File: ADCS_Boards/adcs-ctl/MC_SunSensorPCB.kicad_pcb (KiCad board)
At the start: 4 copper layers, 90.2 x 95.9 mm, 120 parts, among them J1 PC104_Connector, J2 PMOD, J3 Conn_01x03_Female, Q12 20V/0.2A/8MHz/1.2Ω/1Vth, Q14 20V/0.2A/8MHz/1.2Ω/1Vth, Q3 20V/0.2A/8MHz/1.2Ω/1Vth, Q4 20V/0.2A/8MHz/1.2Ω/1Vth, Q6 20V/0.2A/8MHz/1.2Ω/1Vth, Q9 20V/0.2A/8MHz/1.2Ω/1Vth, U1 9DoF IMU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

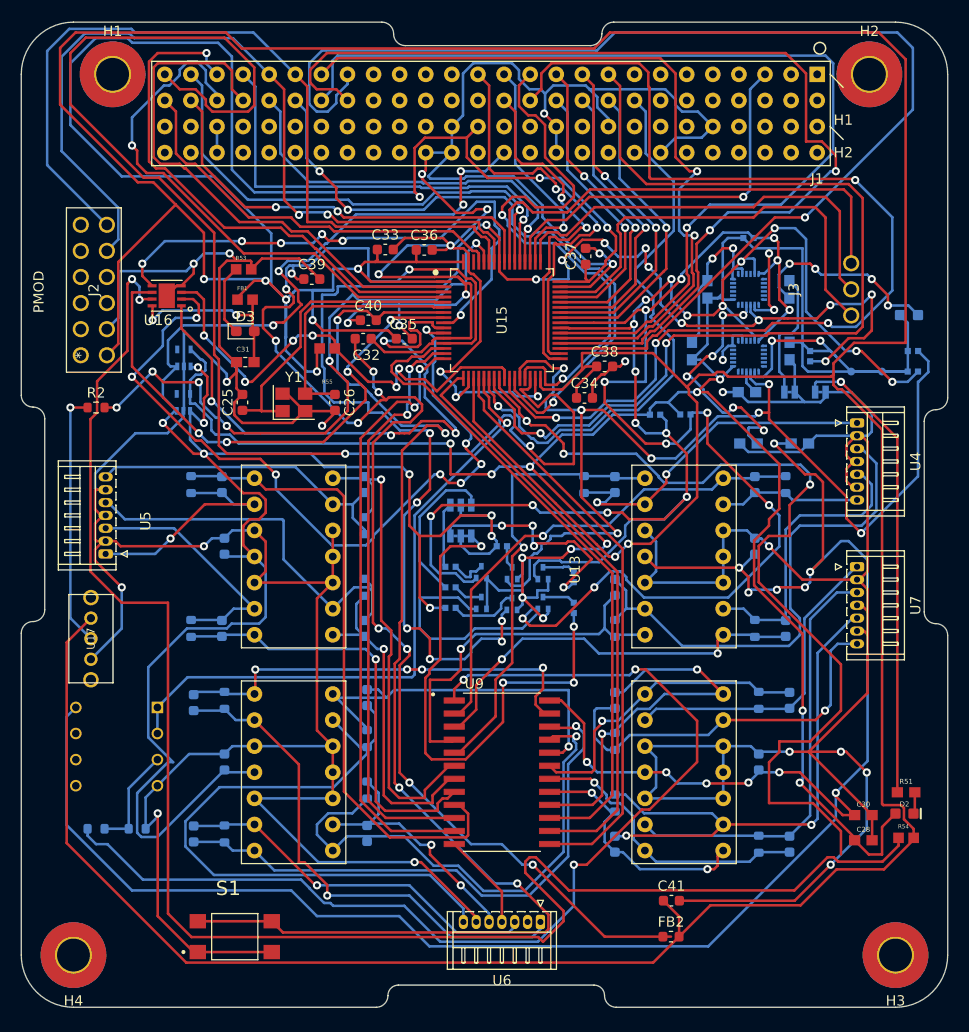
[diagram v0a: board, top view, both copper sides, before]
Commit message: adcs: udpated rwl-db and adcs-ctl on behalf of Yasin
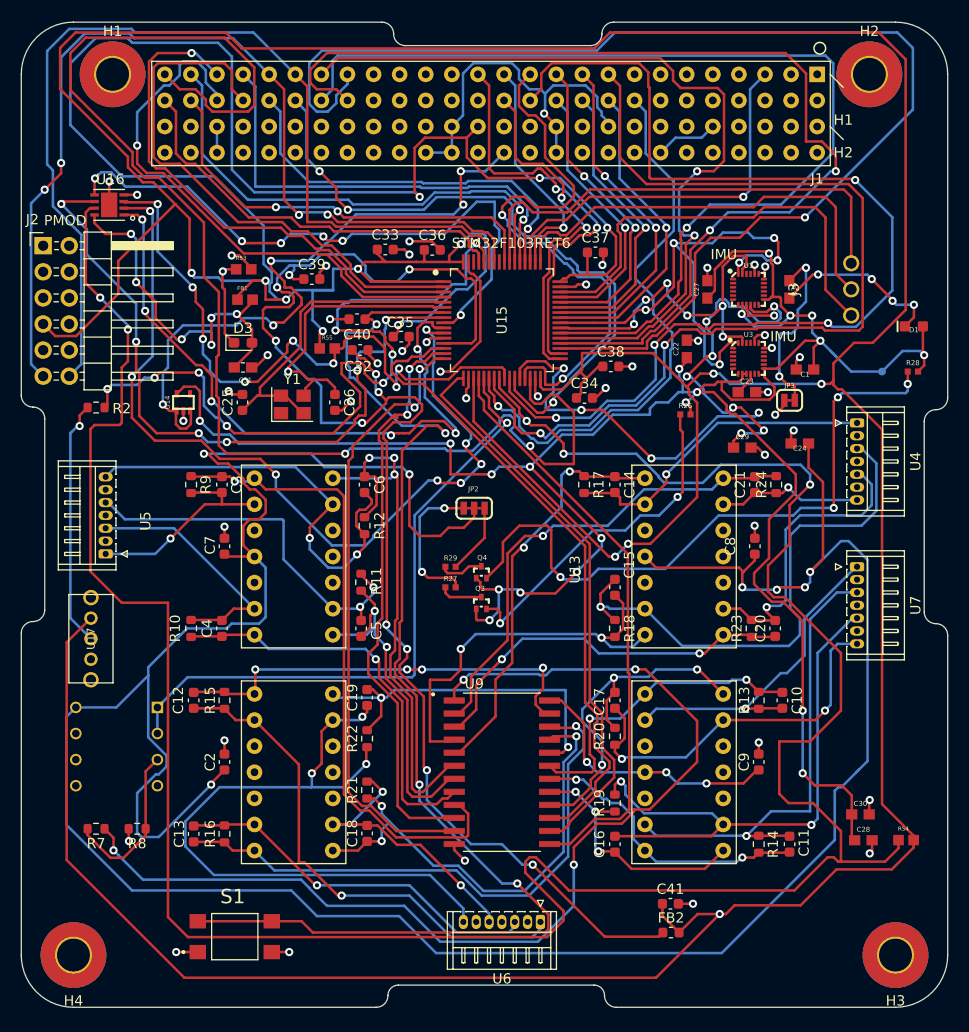
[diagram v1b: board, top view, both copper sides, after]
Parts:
- removed D2: RED, SparkFun_IMU_Breakout_ICM-20948:LED-0603
- removed JP5: I2C PU, SparkFun_IMU_Breakout_ICM-20948:SMT-JUMPER_3_2-NC_TRACE_SILK
- removed JP6: LED, SparkFun_IMU_Breakout_ICM-20948:SMT-JUMPER_2_NC_TRACE_SILK
- removed Q12, Q14, Q6, Q9: 20V/0.2A/8MHz/1.2Ω/1Vth, SparkFun_IMU_Breakout_ICM-20948:SOT-416FL
- removed R1, R3, R32, R33, R40, R43, R46, R47: 2.2k, SparkFun_IMU_Breakout_ICM-20948:0402-TIGHT
- removed R51: 220, SparkFun_IMU_Breakout_ICM-20948:0603
- removed TP2: 1.8V, SparkFun_IMU_Breakout_ICM-20948:PAD.03X.03
- removed U2: 1.8V/100mA, SparkFun_IMU_Breakout_ICM-20948:SC70
- C1, C22, C23, C24, C27, C29, D1, JP2, JP3, Q3, Q4, R26, R27, R28, R29, R36, R7, R8, U1, U14, U3: moved to F.Cu
- C10, C11, C12, C13, C14, C15, C16, C17, C18, C19, C20, C21, C3, C4, C5, C6: value C -> 180pF; moved to F.Cu
- C2, C7, C8, C9: value C -> 100nF; moved to F.Cu
- C25, C26: value 10p -> 10pF
- C31, C32, C34, C35, C36, C37, C38: value 100n -> 100nF
- C33: value 10u -> 10uF
- C39: value 10n -> 10nF
- C40, C41: value 1u -> 1uF
- J2: value PMOD -> PPTC062LJBN-RC; footprint Footprints_QSAT:PPTC062LJBN-RC -> Connector_PinHeader_2.54mm:PinHeader_2x06_P2.54mm_Horizontal
- R10, R11, R12, R13, R14, R15, R16, R17, R18, R19, R20, R21, R22, R23, R24, R9: value R -> 5.76k; moved to F.Cu
- moved J2 11.3 mm to (111.3, 68.8), turned to 0 degrees
- moved U16 10.5 mm to (117.8, 64.8)
- moved C1 2.34 mm to (185.5, 80.8), turned to 180 degrees
- moved JP2 1.33 mm to (153.3, 94.3), turned to 0 degrees
- moved D1 1.20 mm to (196.1, 76.6), turned to 180 degrees
- moved D3 1.14 mm to (130.8, 78.2)
- moved C40 1.14 mm to (142.2, 78.9)
- moved C32 1.10 mm to (141.9, 75.9)
- moved C37 1.02 mm to (165.1, 69.4), turned to 0 degrees
- moved C20 1.02 mm to (182.6, 106.0)
- moved R24 0.92 mm to (182.7, 92.0)
- moved JP3 0.80 mm to (184.0, 83.8), turned to 0 degrees
- moved C36 0.78 mm to (149.2, 69.2)
- moved C29 0.72 mm to (179.4, 88.4), turned to 0 degrees
- moved C10 0.70 mm to (183.3, 113.0)
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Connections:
- C30 pad 1: +5V -> 1.8V
- Q3 pad 2: IMU_SDA -> /SDA/SDI
- Q4 pad 2: IMU_SCL -> /SCL/SCLK
- R26 pad 1: IMU_SDA -> /SDA/SDI
- R28 pad 1: IMU_SCL -> /SCL/SCLK
- U1 pad 9: /AD0/SDO_2 -> GND
- U15 pad 28: /AD0/SDO -> PB2
- U15 pad 57: /AD0/SDO_2 -> PB5
- U3 pad 9: /AD0/SDO -> 1.8V
- Y1 pad 1: RCC_OSC_IN -> unconnected-(Y1-Pad1)
- Y1 pad 2: GND -> RCC_OSC_IN
- Y1 pad 4: GND -> RCC_OSC_IN
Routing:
- net GND: track 692.1 -> 133.5 mm, vias 31 -> 45
- net /AD0/SDO_2: track 144.6 -> 0.00 mm, vias 17 -> 0
- net IMU_SCL: track 142.4 -> 34.7 mm, vias 16 -> 6
- net /AD0/SDO: track 106.3 -> 0.00 mm, vias 7 -> 0
- net IMU_SDA: track 136.8 -> 52.4 mm, vias 11 -> 6
- net /SCL/SCLK: track 0.00 -> 64.1 mm, vias 0 -> 4
- net Net-(JP5-Pad1): track 52.4 -> 0.00 mm, vias 4 -> 0
- net +5V: track 414.7 -> 368.0 mm, vias 24 -> 15
- net Net-(JP6-Pad2): track 45.7 -> 0.00 mm, vias 1 -> 0
- net 1.8V: track 263.6 -> 228.1 mm, vias 16 -> 20
- net PB2: track 0.00 -> 35.1 mm, vias 0 -> 4
- net /SDA/SDI: track 0.00 -> 33.2 mm, vias 0 -> 2
- net Net-(JP5-Pad3): track 22.6 -> 0.00 mm, vias 4 -> 0
- net Net-(C31-Pad2): track 18.0 -> 35.9 mm, vias 2 -> 6
- net SPI1_SCK: track 52.2 -> 69.4 mm, vias 4 -> 6
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
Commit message: Update adcs-ctl for yasin
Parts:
- added C42: 10uF, SparkFun_IMU_Breakout_ICM-20948:0603, F.Cu at (178.6, 140.7)
- added C43: 10uF, SparkFun_IMU_Breakout_ICM-20948:0603, F.Cu at (174.8, 140.7)
- added TP2: 3V3, SparkFun_IMU_Breakout_ICM-20948:PAD.03X.03, F.Cu at (191.6, 134.1)
- added U2: BU33SA5WGWZ-E2, Footprints_QSAT:BU33SA5WGWZ-E2, F.Cu at (184.2, 137.7)
- J2: footprint Connector_PinHeader_2.54mm:PinHeader_2x06_P2.54mm_Horizontal -> Connector_PinSocket_2.54mm:PinSocket_2x06_P2.54mm_Horizontal
- moved J2 11.0 mm to (122.3, 68.5)
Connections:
- J1 pad 79: +3V3 -> unconnected-(J1-Pad79)
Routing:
- net Net-(J1-Pad43): track 92.9 -> 105.7 mm, vias 4 -> 5
- net +5V: track 368.0 -> 375.0 mm, vias 15 -> 16
- net Net-(C31-Pad2): track 35.9 -> 42.1 mm, vias 6 -> 4
- net Net-(J1-Pad41): track 95.5 -> 100.3 mm, vias 0 -> 1
- net GND: track 133.5 -> 137.4 mm, vias 45 -> 48
- net SPI1_MISO: track 84.9 -> 88.7 mm
- net /BOOT0: track 75.3 -> 71.5 mm
- net SPI1_SCK: track 69.4 -> 72.6 mm
- net +3V3: track 631.3 -> 633.6 mm
- net GPIO2: track 63.4 -> 64.5 mm
- net SPI1_NSS: track 64.2 -> 65.1 mm, vias 6 -> 5
- net GPIO1: track 256.6 -> 255.9 mm, vias 5 -> 3

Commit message: adcs: split adcs-ctl board power layer between 5v 3v3 and 1v8
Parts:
- removed JP2: I2C PU, SparkFun_IMU_Breakout_ICM-20948:SMT-JUMPER_3_2-NC_TRACE_SILK
- removed JP3: LED, SparkFun_IMU_Breakout_ICM-20948:SMT-JUMPER_2_NC_TRACE_SILK
- TP1: moved to F.Cu
- moved C43 80.9 mm to (194.7, 62.2)
- moved C41 72.1 mm to (194.8, 64.3)
- moved FB2 70.6 mm to (134.5, 76.1)
- moved U14 62.1 mm to (187.1, 86.5)
- moved C42 57.4 mm to (125.8, 118.2)
- moved C30 54.0 mm to (196.5, 70.4)
- moved C28 53.5 mm to (196.5, 73.4)
- moved Q4 49.5 mm to (197.4, 76.1)
- moved Q3 49.5 mm to (197.2, 79.0)
- moved R27 48.3 mm to (194.9, 81.9), turned to -90 degrees
- moved R29 46.6 mm to (193.9, 81.9), turned to -90 degrees
- moved R26 23.5 mm to (197.1, 81.9), turned to -90 degrees
- moved U2 20.6 mm to (191.4, 118.4)
- moved TP2 10.7 mm to (191.9, 123.3)
- moved D1 9.90 mm to (194.7, 66.8)
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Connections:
- Q3 pad 3: /SDA/SDI_VIN -> IMU_SDA
- Q4 pad 3: /SCL/SCLK_VIN -> IMU_SCL
- R27 pad 1: /SDA/SDI_VIN -> IMU_SDA
- R27 pad 2: Net-(JP2-Pad1) -> +3V3
- R29 pad 1: /SCL/SCLK_VIN -> IMU_SCL
- R29 pad 2: Net-(JP2-Pad3) -> +3V3
- R36 pad 1: Net-(JP3-Pad2) -> GND
- U1 pad 23: IMU_SCL -> /SCL/SCLK
- U1 pad 24: IMU_SDA -> /SDA/SDI
- U3 pad 23: IMU_SCL -> /SCL/SCLK
- U3 pad 24: IMU_SDA -> /SDA/SDI
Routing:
- net +3V3: track 633.6 -> 82.5 mm, vias 15 -> 22
- net +5V: track 375.0 -> 29.7 mm, vias 16 -> 15
- net 1.8V: track 228.1 -> 24.2 mm, vias 20 -> 14
- net +3.3VA: track 144.7 -> 64.5 mm, vias 11 -> 6
- net GND: track 137.4 -> 165.5 mm, vias 48 -> 93
- net GPIO1: track 255.9 -> 230.5 mm
- net PB0: track 104.5 -> 123.6 mm
- net Net-(JP3-Pad2): track 17.8 -> 0.00 mm, vias 2 -> 0
- net IMU_SCL: track 34.7 -> 51.1 mm, vias 6 -> 5
- net /SCL/SCLK: track 64.1 -> 47.9 mm
- net Net-(JP2-Pad1): track 14.3 -> 0.00 mm, vias 2 -> 0
- net Net-(JP2-Pad3): track 6.87 -> 0.00 mm
- net /SCL/SCLK_VIN: track 4.27 -> 0.00 mm
- net /SDA/SDI_VIN: track 4.22 -> 0.00 mm
- net /SDA/SDI: track 33.2 -> 36.7 mm, vias 2 -> 3
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- added copper zone on In2.Cu, net +3V3
- added copper zone on In2.Cu, net 1.8V

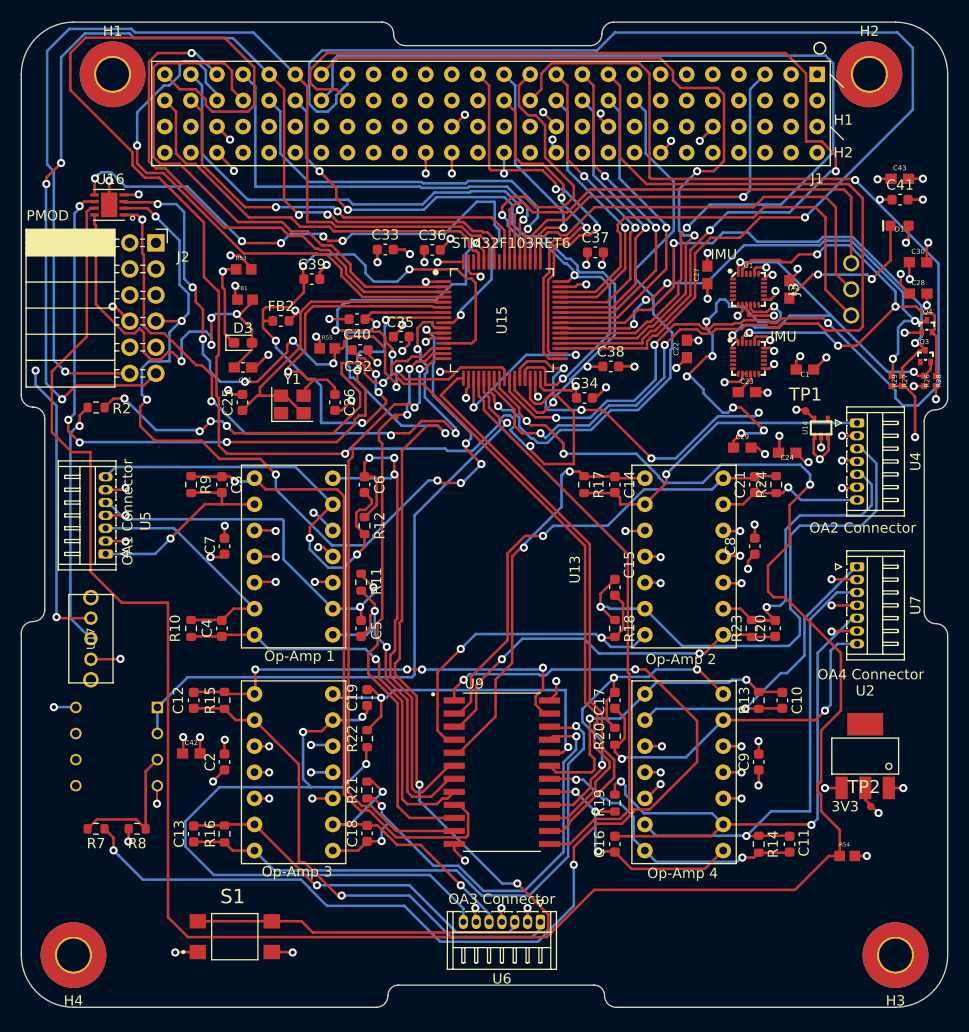
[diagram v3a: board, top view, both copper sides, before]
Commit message: adcs: adcs-ctl: continued silkscreen changes
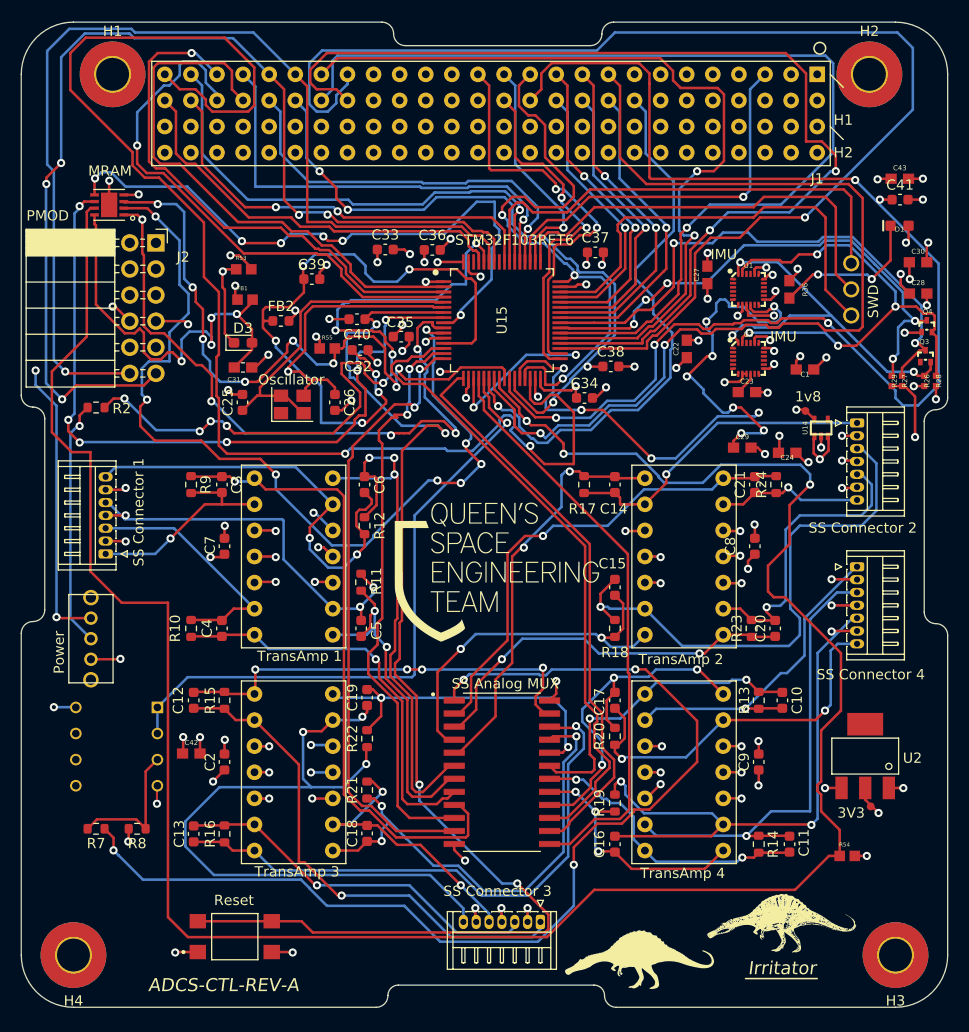
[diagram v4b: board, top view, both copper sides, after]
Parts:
- added G***: LOGO, LOGO, F.Cu at (183.3, 134.7)
- added G***: LOGO, LOGO, F.Cu at (155.6, 100.3)
- added G***: LOGO, LOGO, F.Cu at (169.4, 138.3)
- added G***: LOGO, LOGO, B.Cu at (175.3, 134.1)
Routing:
- net GND: track 165.5 -> 148.1 mm, vias 93 -> 83
- net +5V: track 29.7 -> 27.7 mm, vias 15 -> 14
- net Net-(C19-Pad2): track 36.2 -> 34.4 mm
- net +3V3: track 82.5 -> 83.3 mm
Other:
- board text added: "1v8"
- board text added: "ADCS-CTL-REV-A"
- board text added: "Alex MacQuarrie"
- board text added: "Ankylosaurus"
- board text added: "Irritator"
- board text added: "MRAM"
- board text added: "Oscillator"
- board text added: "Power"
- board text added: "Reset"
- board text added: "SS 3v3 Limiter"
- board text added: "SS Analog MUX"
- board text added: "SWD"
- board text added: "Yasin Shahrami Tony Jajcanin Aidan Darling Hatim Belhadjhamida Luke Parna-Gile Alex MacQuarrie Dylan Burke Sid Arya Aidan Sheedy"
- board text added: "ptd-db"
